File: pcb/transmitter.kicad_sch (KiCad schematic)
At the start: 52 parts, among them J6 Conn_Coaxial, SW2 SW_DIP_x04, U10 MIC5504-3.3YM5, U9 STM32WL55CCUx, Y1 Crystal, Y2 Crystal_GND23

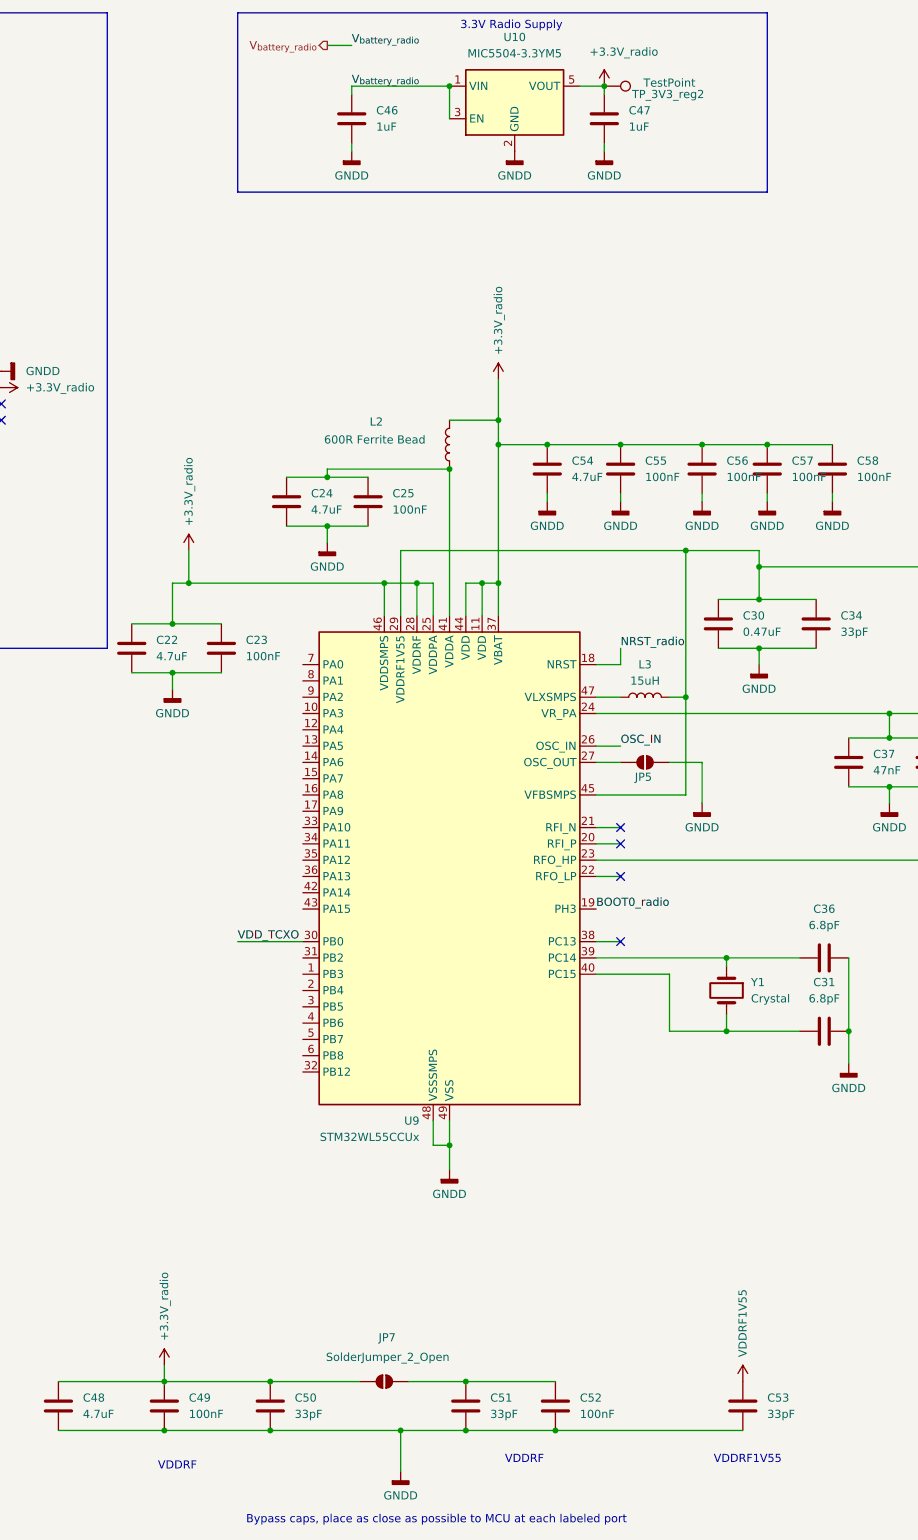
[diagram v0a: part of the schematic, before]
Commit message: Backup
Backup before board layer change from 4-2 in case of lost components
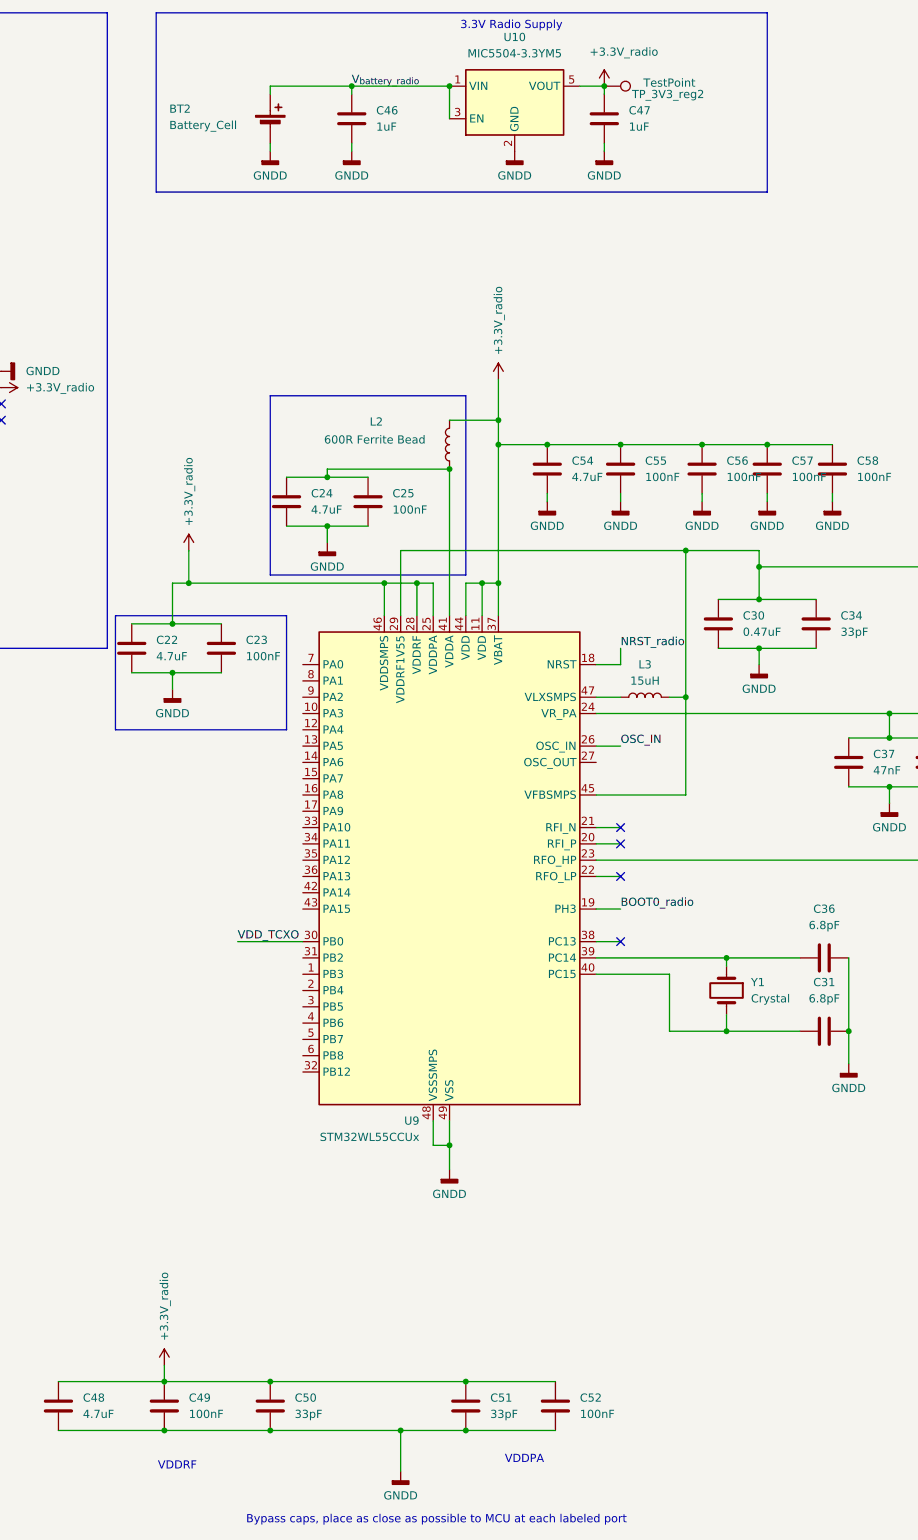
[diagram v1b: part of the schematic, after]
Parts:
- removed C53: 33pF, Capacitor_SMD:C_0402_1005Metric, symbol Device:C
- removed JP5: ~, Jumper:SolderJumper-2_P1.3mm_Open_RoundedPad1.0x1.5mm, symbol Jumper:SolderJumper_2_Open
- removed JP7: SolderJumper_2_Open, Jumper:SolderJumper-2_P1.3mm_Open_RoundedPad1.0x1.5mm, symbol Jumper:SolderJumper_2_Open
- added BT2: Battery_Cell, Connector_JST:JST_PH_S2B-PH-K_1x02_P2.00mm_Horizontal, symbol Device:Battery_Cell
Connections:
- net +3.3V_radio: now also C51.1, C52.1
- net GNDD: now also BT2.2 (-)
- net V_{battery_radio}: now also BT2.1 (+)
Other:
- note added: "VDDPA"
- note removed: "VDDRF1V55"

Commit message: Pre-fab update
Pre fab update
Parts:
- removed C49: 100nF, Capacitor_SMD:C_0402_1005Metric, symbol Device:C
- removed JP3, JP4: SolderJumper_2_Open, Jumper:SolderJumper-2_P1.3mm_Open_RoundedPad1.0x1.5mm, symbol Jumper:SolderJumper_2_Open
- renumbered TP_3V3_reg2 to 3V3_reg2
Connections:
- net SWO_radio: now reaches U9.1 (PB3)
- net TIMEPULSE_IN: now reaches U9.13 (PA5)
- net SPI1_MISO_radio: now reaches U9.2 (PB4)
- net SPI1_MOSI_radio: now reaches U9.3 (PB5)
- net SWDIO_radio: now reaches U9.36 (PA13)
- net USART1_TX_radio: now reaches U9.4 (PB6)
- net SWCLK_radio: now reaches U9.42 (PA14)
- net USART1_RX_radio: now reaches U9.5 (PB7)
- net SPI1_CS_radio: now reaches U9.7 (PA0)
- net SPI1_SCK_radio: now reaches U9.8 (PA1)
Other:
- moved on the sheet: C22, C23, RN3, SW2
